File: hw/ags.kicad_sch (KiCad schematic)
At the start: 16 parts, among them J1 Screw_Terminal_01x08, SW1 SW_MEC_5E, U12 NV24C08DWVLT3G, U5 ESP32-S3-MINI-1

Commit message: Footprints created, starting layout
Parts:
- D1: footprint (none) -> qmi_footprints:B38G3RGB-10D0003H2U1930
- J1: footprint (none) -> qmi_footprints:QT08ASF83H0000G
- SW1: value SW_MEC_5E -> PTS526SM15SMTR2 LFS; footprint (none) -> qmi_footprints:SON4_PTS526 SM15 SMTR2 LFS_CNK
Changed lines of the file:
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@@
 			)
 		)
-		(property "Footprint" ""
+		(property "Footprint" "qmi_footprints:B38G3RGB-10D0003H2U1930"
 			(at 106.68 81.28 0)
 			(effects
@@
 			)
 		)
-		(property "Footprint" ""
+		(property "Footprint" "qmi_footprints:QT08ASF83H0000G"
 			(at 219.71 137.16 0)
 			(effects
@@
 			)
 		)
-		(property "Value" "SW_MEC_5E"
-			(at 88.9 107.95 90)
-			(effects
-				(font
-					(size 1.27 1.27)
-				)
-			)
-		)
-		(property "Footprint" ""
+		(property "Value" "PTS526SM15SMTR2 LFS"
+			(at 95.25 108.204 90)
+			(effects
+				(font
+					(size 1.27 1.27)
+				)
+			)
+		)
+		(property "Footprint" "qmi_footprints:SON4_PTS526 SM15 SMTR2 LFS_CNK"
 			(at 87.63 102.87 0)
 			(effects
@@
 			)
 		)
-		(property "Datasheet" "http://www.apem.com/int/index.php?controller=attachment&id_attachment=1371"
+		(property "Datasheet" ""
 			(at 87.63 102.87 0)
 			(effects
@@
 			)
 		)
-		(property "Description" "MEC 5E single pole normally-open tactile switch"
+		(property "Description" ""
 			(at 80.01 102.87 0)
 			(effects

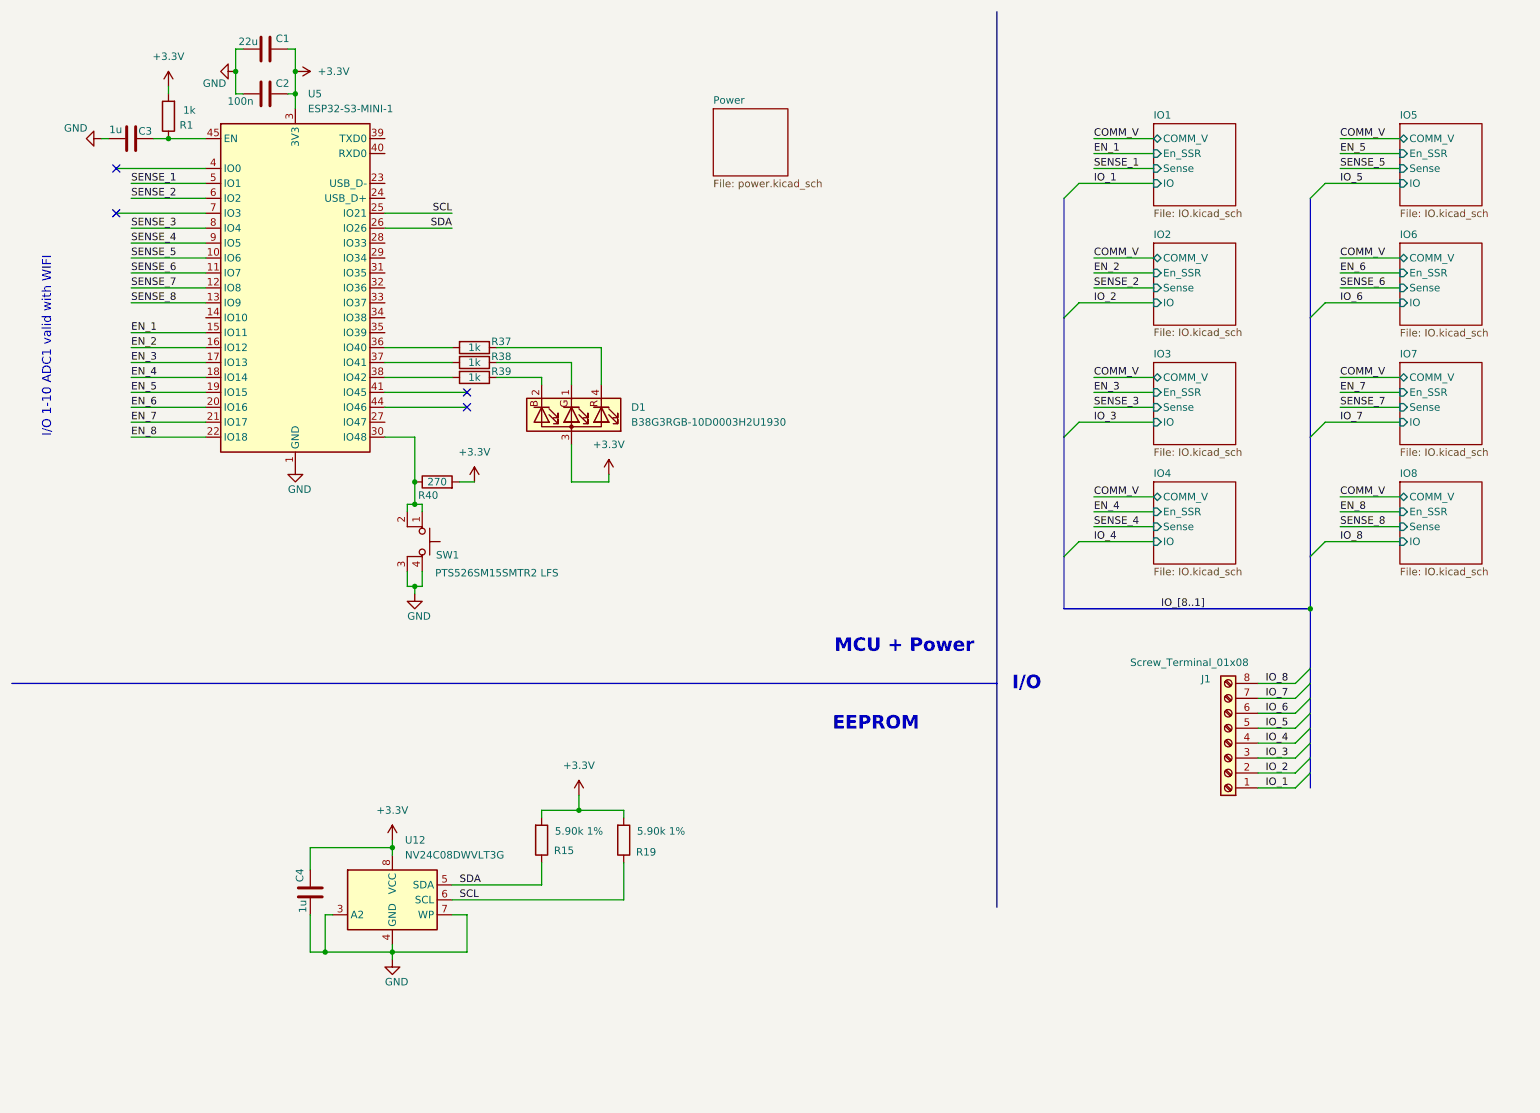
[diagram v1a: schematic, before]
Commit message: All parts placed and routed
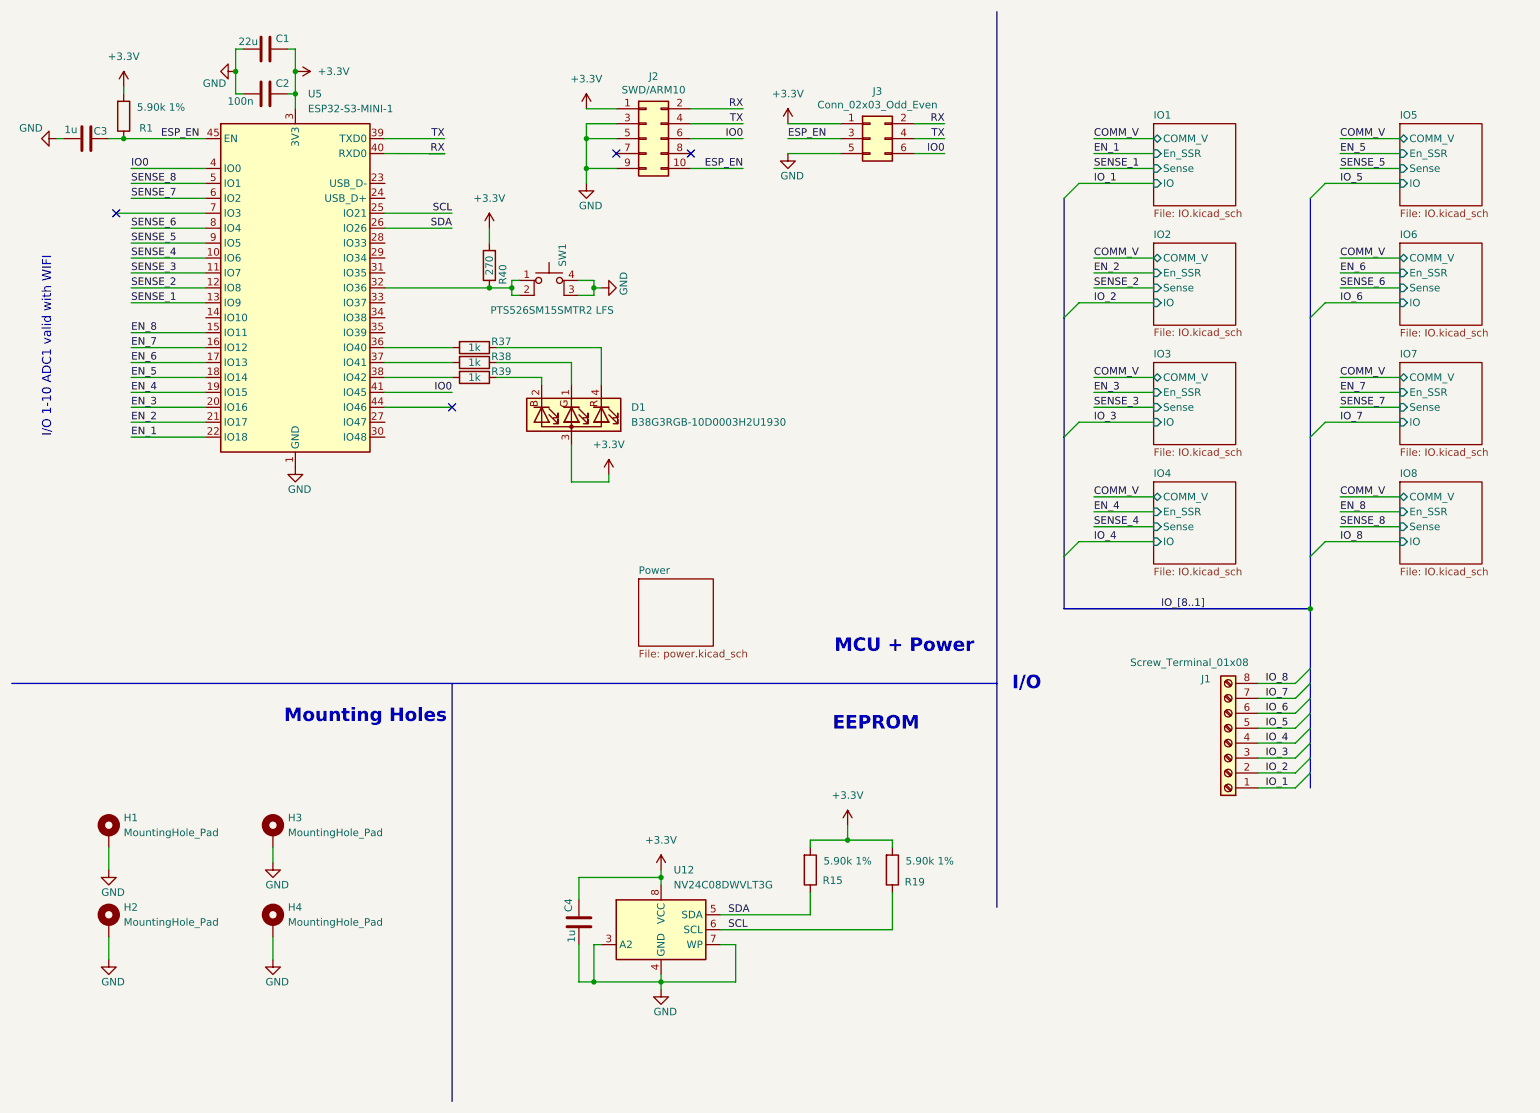
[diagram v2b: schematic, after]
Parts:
- added H1, H2, H3, H4: MountingHole_Pad, MountingHole:MountingHole_3.2mm_M3_ISO7380_Pad, symbol Mechanical:MountingHole_Pad
- added J2: SWD/ARM10, Connector_PinHeader_1.27mm:PinHeader_2x05_P1.27mm_Vertical_SMD, symbol Connector_Generic:Conn_02x05_Odd_Even
- added J3: Conn_02x03_Odd_Even, Connector:Tag-Connect_TC2030-IDC-NL_2x03_P1.27mm_Vertical, symbol Connector_Generic:Conn_02x03_Odd_Even
- C1: footprint Capacitor_SMD:C_0603_1608Metric -> Capacitor_SMD:C_0805_2012Metric
- R1: value 1k -> 5.90k 1%
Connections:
- net +3.3V: now also J2.1 (Pin_1), J3.1 (Pin_1)
- net EN_1: now also U5.22 (IO18); no longer U5.15 (IO11)
- net EN_2: now also U5.21 (IO17); no longer U5.16 (IO12)
- net EN_3: now also U5.20 (IO16); no longer U5.17 (IO13)
- net EN_4: now also U5.19 (IO15); no longer U5.18 (IO14)
- net EN_5: now also U5.18 (IO14); no longer U5.19 (IO15)
- net EN_6: now also U5.17 (IO13); no longer U5.20 (IO16)
- net EN_7: now also U5.16 (IO12); no longer U5.21 (IO17)
- net EN_8: now also U5.15 (IO11); no longer U5.22 (IO18)
- net GND: now also H1.1, H2.1, H3.1, H4.1, J2.3 (Pin_3), J2.5 (Pin_5), J2.9 (Pin_9), J3.5 (Pin_5)
- net SENSE_1: now also U5.13 (IO9); no longer U5.5 (IO1)
- net SENSE_2: now also U5.12 (IO8); no longer U5.6 (IO2)
- net SENSE_3: now also U5.11 (IO7); no longer U5.8 (IO4)
- net SENSE_4: now also U5.10 (IO6); no longer U5.9 (IO5)
- net SENSE_5: now also U5.9 (IO5); no longer U5.10 (IO6)
- net SENSE_6: now also U5.8 (IO4); no longer U5.11 (IO7)
- net SENSE_7: now also U5.6 (IO2); no longer U5.12 (IO8)
- net SENSE_8: now also U5.5 (IO1); no longer U5.13 (IO9)
- net ESP_EN: now reaches C3.2, R1.1, U5.45 (EN)
- net ESP_EN: now also J2.10 (Pin_10), J3.3 (Pin_3)
- net at R40.1, SW1.1, SW1.2: now also U5.32 (IO36); no longer U5.30 (IO48)
- net TX: now reaches U5.39 (TXD0)
- net TX: now also J2.4 (Pin_4), J3.4 (Pin_4)
- net IO0: now reaches U5.4 (IO0)
- net IO0: now also U5.41 (IO45), J2.6 (Pin_6), J3.6 (Pin_6)
- net RX: now reaches U5.40 (RXD0)
- net RX: now also J2.2 (Pin_2), J3.2 (Pin_2)
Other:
- note added: "Mounting Holes"
- moved on the sheet: C3, C4, R15, R19, R40, SW1, U12

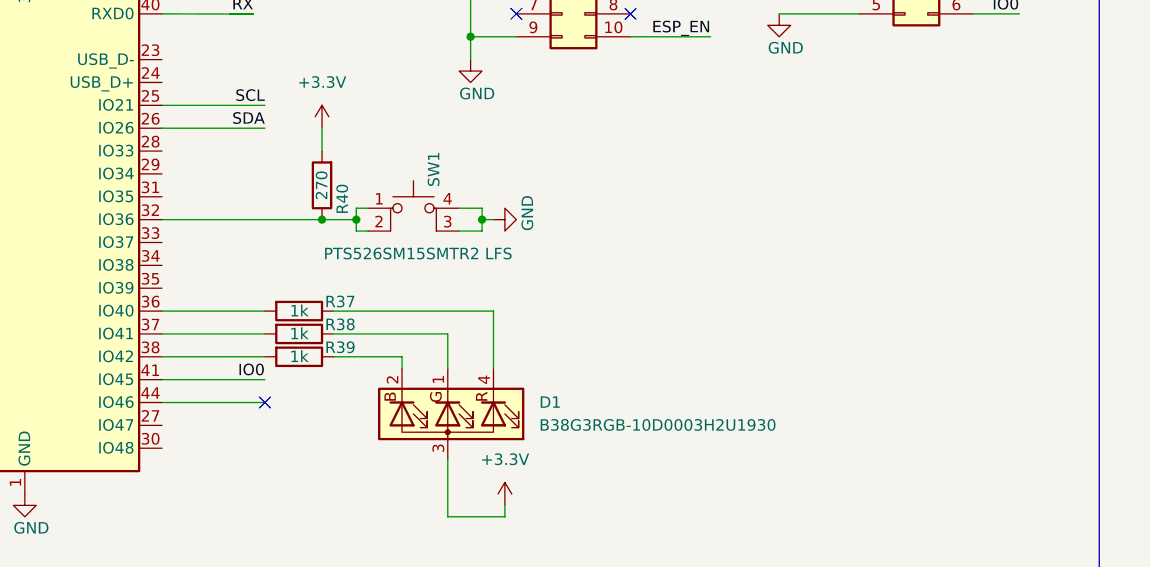
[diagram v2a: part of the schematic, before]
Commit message: Added spare pins breakout to header, cleaned up silk
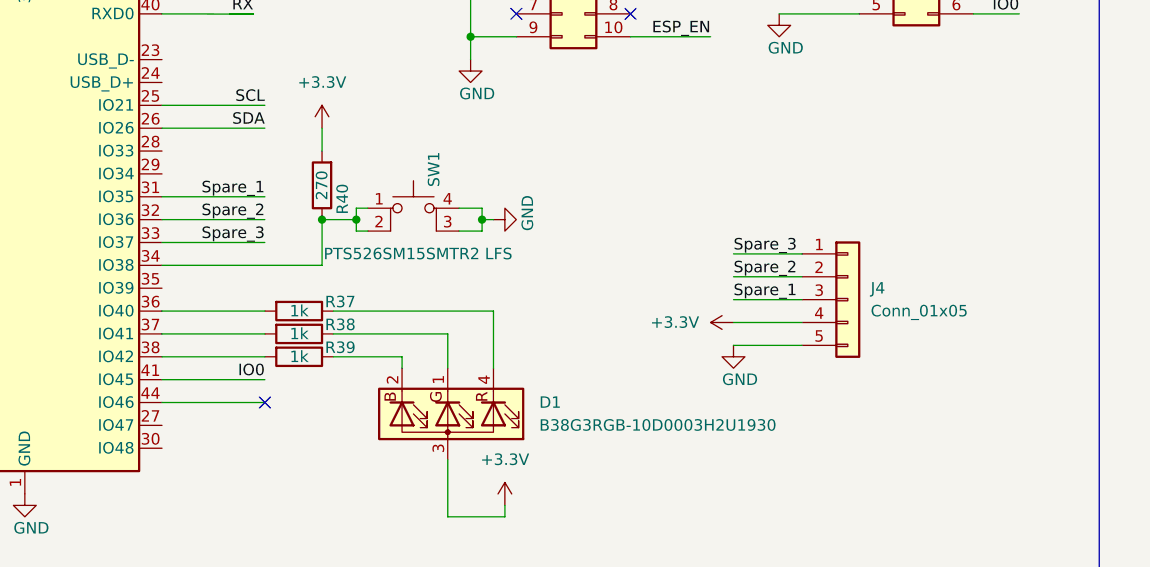
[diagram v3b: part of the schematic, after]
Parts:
- added J4: Conn_01x05, Connector_PinSocket_2.54mm:PinSocket_1x05_P2.54mm_Vertical, symbol Connector_Generic:Conn_01x05
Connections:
- net +3.3V: now also J4.4 (Pin_4)
- net GND: now also J4.5 (Pin_5)
- net at R40.1, SW1.1, SW1.2: now also U5.34 (IO38); no longer U5.32 (IO36)
- net Spare_1: now reaches U5.31 (IO35)
- net Spare_1: now also J4.3 (Pin_3)
- net Spare_3: now reaches U5.33 (IO37)
- net Spare_3: now also J4.1 (Pin_1)
- new net Spare_2: J4.2 (Pin_2), U5.32 (IO36)
